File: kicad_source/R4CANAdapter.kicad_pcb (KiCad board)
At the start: 2 copper layers, 47.5 x 51 mm, 31 parts, among them CN1 CONN_01X05, CN2 691322310004, CN3 GH_SM04B-GHS-TB, CN4 GH_SM04B-GHS-TB, CN5 SM04B-SRSS-TB, Q1 2N7002, Q2 2N7002, U1 MCP2551-I/SN, U2 24LC64

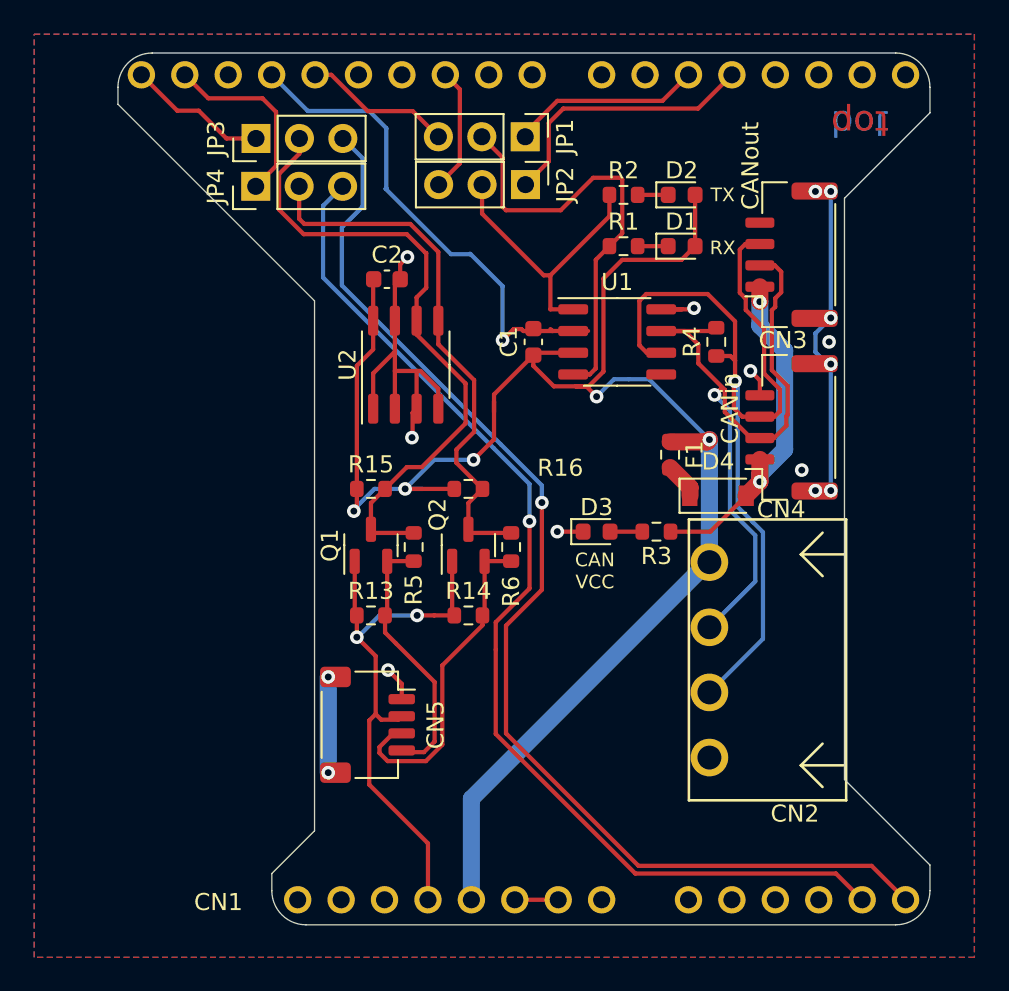
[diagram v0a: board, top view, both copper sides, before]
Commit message: added jumper for CAN termination
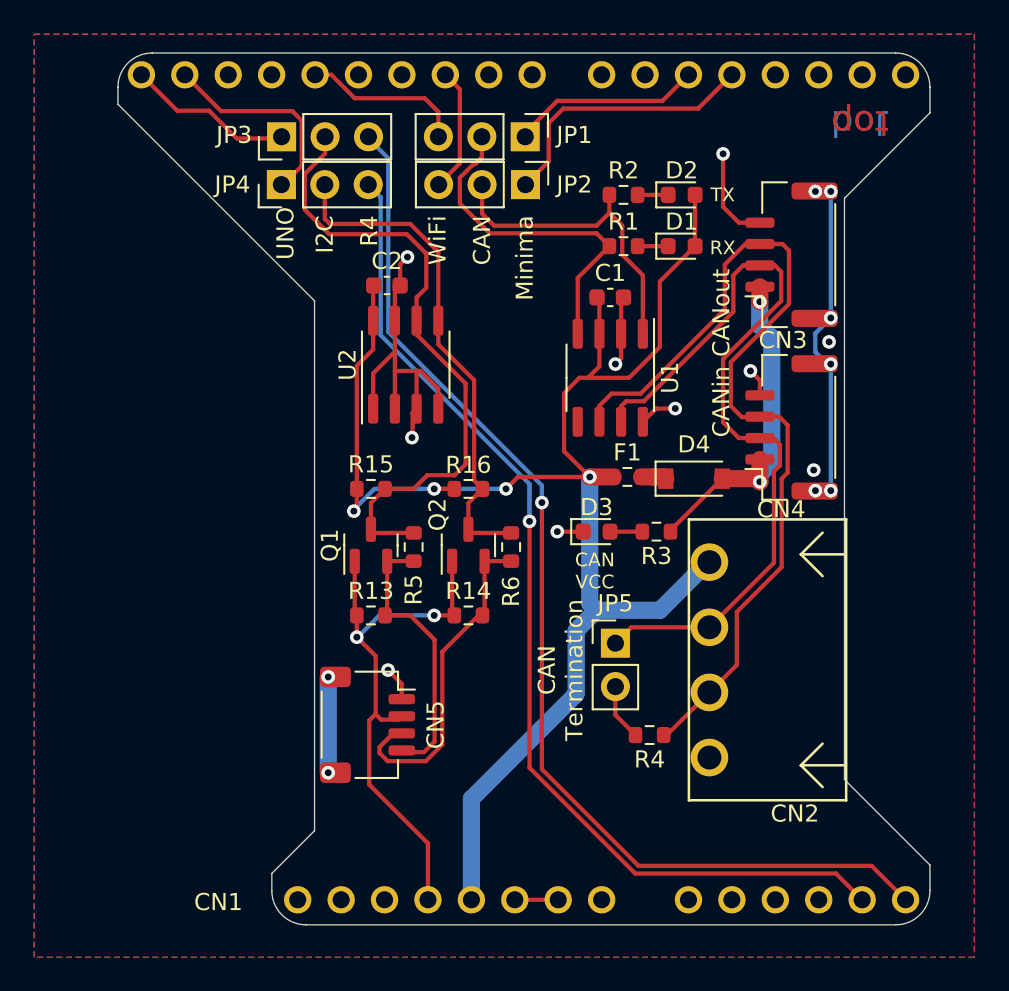
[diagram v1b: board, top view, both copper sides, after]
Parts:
- added JP5: Jumper_2_Open, Connector_PinHeader_2.54mm:PinHeader_1x02_P2.54mm_Vertical, F.Cu at (146.6, 121.0)
- R4: value DNI -> 120R
- moved R4 23.3 mm to (148.6, 126.4), turned to 180 degrees
- moved C1 5.20 mm to (146.3, 100.8), turned to 0 degrees
- moved F1 2.82 mm to (147.3, 111.3), turned to 0 degrees
- moved U1 2.14 mm to (146.3, 105.5), turned to -90 degrees
- moved D4 1.72 mm to (151.2, 111.4)
- moved JP3 1.50 mm to (127.1, 91.4)
- moved JP4 1.50 mm to (127.1, 94.2)
- moved C2 0.36 mm to (133.2, 100.1)
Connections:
- R4 pad 2: /CANH -> Net-(R4-Pad2)
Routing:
- net GND: track 61.6 -> 40.9 mm, vias 9 -> 10
- net +5V: track 103.7 -> 94.7 mm, vias 5 -> 4
- net /CAN_RX: track 25.7 -> 20.2 mm
- net /CANH: track 42.4 -> 47.4 mm, vias 1 -> 0
- net /R4_SCL: track 68.9 -> 65.5 mm
- net Net-(R4-Pad2): track 0.00 -> 3.32 mm
- net /R4_SDA: track 63.8 -> 60.7 mm
- net /I2C_SDA: track 31.9 -> 29.6 mm
- net /CAN_TX: track 16.6 -> 18.7 mm
- net /ARDUINO_SCL: track 8.25 -> 9.75 mm
- net /CANL: track 51.8 -> 53.2 mm, vias 1 -> 0
- net /ARDUINO_SDA: track 11.1 -> 12.3 mm
- net /I2C_SCL_3V: track 15.6 -> 16.4 mm
- net /CAN_RX_WIFI: track 8.72 -> 9.57 mm
- net /CANVCC_F: track 2.13 -> 1.47 mm
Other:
- board text added: "CAN"
- board text added: "CAN Termination"
- board text added: "I2C"
- board text added: "Minima"
- board text added: "R4"
- board text added: "R4CANAdapter 0.1"
- board text added: "UNO"
- board text added: "WiFi"
- board text removed: "3V3"
- board text removed: "5V"
- board text removed: "CAN RX"
- board text removed: "CAN TX"
- board text removed: "Dronecode CANAdapter 0.2"

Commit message: added some labels, beautified layout, made DRC
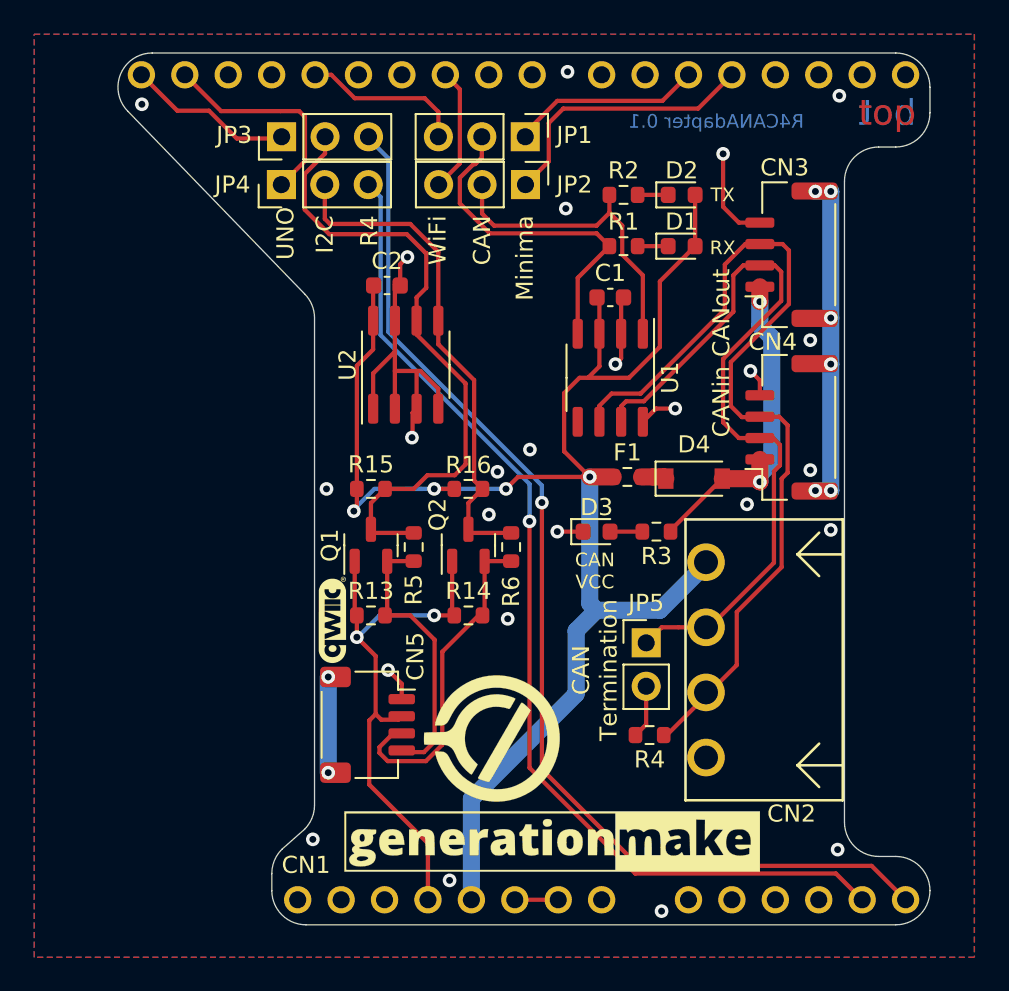
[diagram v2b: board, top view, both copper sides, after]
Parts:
- added L2: Label, generationmake:generationmake_logo, F.Cu at (142.9, 137.9)
- added L3: Label, generationmake:opencyphal_small, F.Cu at (139.4, 126.6)
- added L4: Label, generationmake:qwiic_logo, F.Cu at (130.0, 119.7)
- moved L1 9.91 mm to (140.5, 104.6), turned to 180 degrees
- moved JP5 1.80 mm to (148.4, 121.0)
- moved CN2 0.20 mm to (151.9, 122.0)
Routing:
- net /CANH: track 47.4 -> 45.6 mm
- net /MP: track 18.4 -> 19.3 mm
- net GND: vias 10 -> 25
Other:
- outline, holes or cut-outs redrawn

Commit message: updated images
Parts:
- U1, U2: footprint Package_SO:SO-8_3.9x4.9mm_P1.27mm -> Package_SO:SOIC-8_3.9x4.9mm_P1.27mm
